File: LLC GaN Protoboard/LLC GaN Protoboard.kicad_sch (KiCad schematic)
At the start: 0 parts

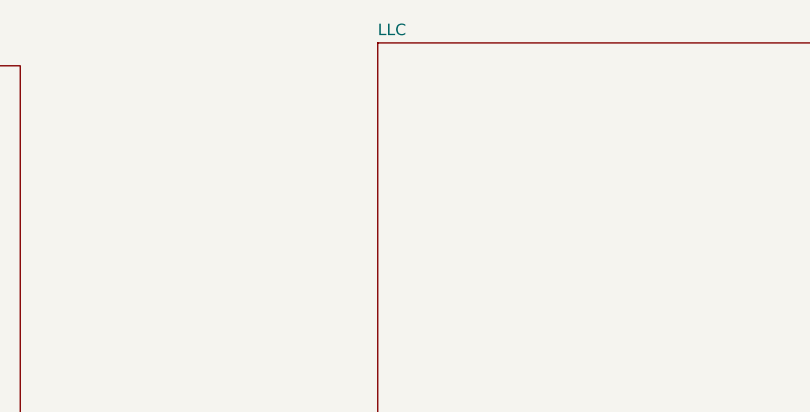
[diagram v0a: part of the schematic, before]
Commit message: Added more calculations
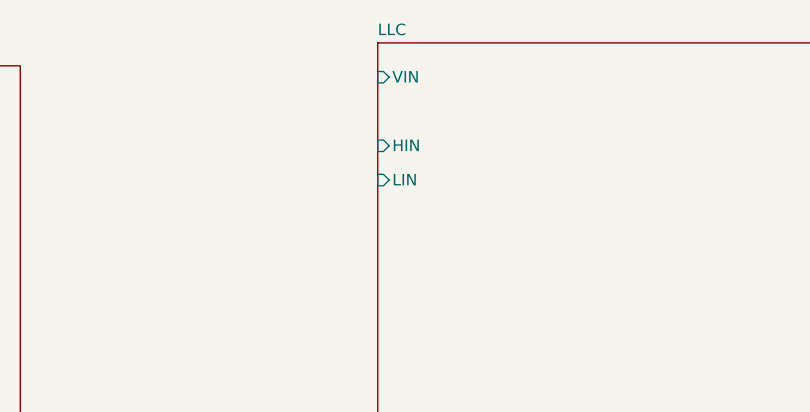
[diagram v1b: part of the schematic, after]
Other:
- sheet LLC ports: added HIN, LIN, VIN; removed none
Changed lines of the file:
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@@
+			)
+		)
+		(pin "HIN" input
+			(at 137.16 38.1 180)
+			(effects
+				(font
+					(size 1.27 1.27)
+				)
+				(justify left)
+			)
+		)
+		(pin "LIN" input
+			(at 137.16 41.91 180)
+			(effects
+				(font
+					(size 1.27 1.27)
+				)
+				(justify left)
+			)
+		)
+		(pin "VIN" input
+			(at 137.16 30.48 180)
+			(effects
+				(font
+					(size 1.27 1.27)
+				)
+				(justify left)
 			)
 		)

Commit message: Finished schematic
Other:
- sheet LLC ports: added IIN_HIGH, IIN_LOW, IOUT_HIGH, IOUT_LOW, VIN_RECT, VOUT; removed none
- sheet Mount ports: added ADCINA4/VIN, ADCINA9/IIN, ADCINB4/VOUT, ADCINB5/IOUT, PWM7A/HI, PWM7B/LO, SPIB_CLK, SPIB_PICO, SPIB_POCI; removed none
- sheet Sense ports: added ADC_IIN, ADC_IOUT, ADC_VIN, ADC_VOUT, INV_SHUNT_HIGH, INV_SHUNT_LOW, VIN, VOUT; removed none
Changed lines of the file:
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@@
 	(paper "A4")
 	(sheet
-		(at 38.1 133.35)
+		(at 34.29 144.78)
 		(size 119.38 44.45)
 		(exclude_from_sim no)
@@
 		)
 		(property "Sheetname" "Sense"
-			(at 38.1 132.6384 0)
+			(at 34.29 144.0684 0)
 			(show_name no)
 			(do_not_autoplace no)
@@
 		)
 		(property "Sheetfile" "Sense.kicad_sch"
-			(at 38.1 178.3846 0)
+			(at 34.29 189.8146 0)
 			(show_name no)
 			(do_not_autoplace no)
@@
 				)
 				(justify left top)
+			)
+		)
+		(pin "ADC_IIN" input
+			(at 34.29 147.32 180)
+			(effects
+				(font
+					(size 1.27 1.27)
+				)
+				(justify left)
+			)
+		)
+		(pin "ADC_IOUT" input
+			(at 34.29 149.86 180)
+			(effects
+				(font
+					(size 1.27 1.27)
+				)
+				(justify left)
+			)
+		)
+		(pin "ADC_VIN" input
+			(at 34.29 152.4 180)
+			(effects
+				(font
+					(size 1.27 1.27)
+				)
+				(justify left)
+			)
+		)
+		(pin "ADC_VOUT" input
+			(at 34.29 154.94 180)
+			(effects
+				(font
+					(size 1.27 1.27)
+				)
+				(justify left)
+			)
+		)
+		(pin "INV_SHUNT_HIGH" input
+			(at 34.29 157.48 180)
+			(effects
+				(font
+					(size 1.27 1.27)
+				)
+				(justify left)
+			)
+		)
+		(pin "INV_SHUNT_LOW" input
+			(at 34.29 160.02 180)
+			(effects
+				(font
+					(size 1.27 1.27)
+				)
+				(justify left)
+			)
+		)
+		(pin "VIN" input
+			(at 34.29 162.56 180)
+			(effects
+				(font
+					(size 1.27 1.27)
+				)
+				(justify left)
+			)
+		)
+		(pin "VOUT" input
+			(at 34.29 165.1 180)
+			(effects
+				(font
+					(size 1.27 1.27)
+				)
+				(justify left)
 			)
 		)
@@
 			)
 		)
+		(pin "ADCINA4{slash}VIN" input
+			(at 28.8607 40.64 180)
+			(effects
+				(font
+					(size 1.27 1.27)
+				)
+				(justify left)
+			)
+		)
+		(pin "ADCINA9{slash}IIN" input
+			(at 28.8607 43.18 180)
+			(effects
+				(font
+					(size 1.27 1.27)
+				)
+				(justify left)
+			)
+		)
+		(pin "ADCINB4{slash}VOUT" input
+			(at 28.8607 45.72 180)
+			(effects
+				(font
+					(size 1.27 1.27)
+				)
+				(justify left)
+			)
+		)
+		(pin "ADCINB5{slash}IOUT" input
+			(at 28.8607 48.26 180)
+			(effects
+				(font
+					(size 1.27 1.27)
+				)
+				(justify left)
+			)
+		)
+		(pin "PWM7A{slash}HI" input
+			(at 28.8607 50.8 180)
+			(effects
+				(font
+					(size 1.27 1.27)
+				)
+				(justify left)
+			)
+		)
+		(pin "PWM7B{slash}LO" input
+			(at 28.8607 53.34 180)
+			(effects
+				(font
+					(size 1.27 1.27)
+				)
+				(justify left)
+			)
+		)
+		(pin "SPIB_CLK" input
+			(at 28.8607 55.88 180)
+			(effects
+				(font
+					(size 1.27 1.27)
+				)
+				(justify left)
+			)
+		)
+		(pin "SPIB_PICO" input
+			(at 28.8607 58.42 180)
+			(effects
+				(font
+					(size 1.27 1.27)
+				)
+				(justify left)
+			)
+		)
+		(pin "SPIB_POCI" input
+			(at 28.8607 60.96 180)
+			(effects
+				(font
+					(size 1.27 1.27)
+				)
+				(justify left)
+			)
+		)
 		(instances
 			(project "LLC GaN Protoboard"
@@
 	)
 	(sheet
-		(at 137.16 26.67)
+		(at 172.72 26.67)
 		(size 97.79 82.55)
 		(exclude_from_sim no)
@@
 		)
 		(property "Sheetname" "LLC"
-			(at 137.16 25.9584 0)
+			(at 172.72 25.9584 0)
 			(show_name no)
 			(do_not_autoplace no)
@@
 		)
 		(property "Sheetfile" "LLC.kicad_sch"
-			(at 137.16 109.8046 0)
+			(at 172.72 109.8046 0)
 			(show_name no)
 			(do_not_autoplace no)
@@
 		)
 		(pin "HIN" input
-			(at 137.16 38.1 180)
+			(at 172.72 38.1 180)
 			(effects
 				(font
@@
 		)
 		(pin "LIN" input
-			(at 137.16 41.91 180)
+			(at 172.72 41.91 180)
 			(effects
 				(font
@@
 		)
 		(pin "VIN" input
-			(at 137.16 30.48 180)
-			(effects
-				(font
+			(at 172.72 30.48 180)
+			(effects
+				(font
+					(size 1.27 1.27)
+				)
+				(justify left)
+			)
+		)
+		(pin "IIN_HIGH" input
+			(at 172.72 44.45 180)
+			(effects
+				(font
+					(size 1.27 1.27)
+				)
+				(justify left)
+			)
+		)
+		(pin "IIN_LOW" input
+			(at 172.72 46.99 180)
+			(effects
+				(font
+					(size 1.27 1.27)
+				)
+				(justify left)
+			)
+		)
+		(pin "IOUT_HIGH" input
+			(at 172.72 49.53 180)
+			(effects
+				(font
+					(size 1.27 1.27)
+				)
+				(justify left)
+			)
+		)
+		(pin "IOUT_LOW" input
+			(at 172.72 52.07 180)
+			(effects
+				(font
+					(size 1.27 1.27)
+				)
+				(justify left)
+			)
+		)
+		(pin "VIN_RECT" input
+			(at 172.72 54.61 180)
+			(effects
+				(font
+					(size 1.27 1.27)
+				)
+				(justify left)
+			)
+		)
+		(pin "VOUT" input
+			(at 172.72 57.15 180)
+			(effects
+				(font

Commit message: Edited schematic
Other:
- sheet Mount ports: added none; removed SPIB_CLK, SPIB_PICO, SPIB_POCI
- sheet Sense ports: added IOUT_HIGH, IOUT_LOW; removed none

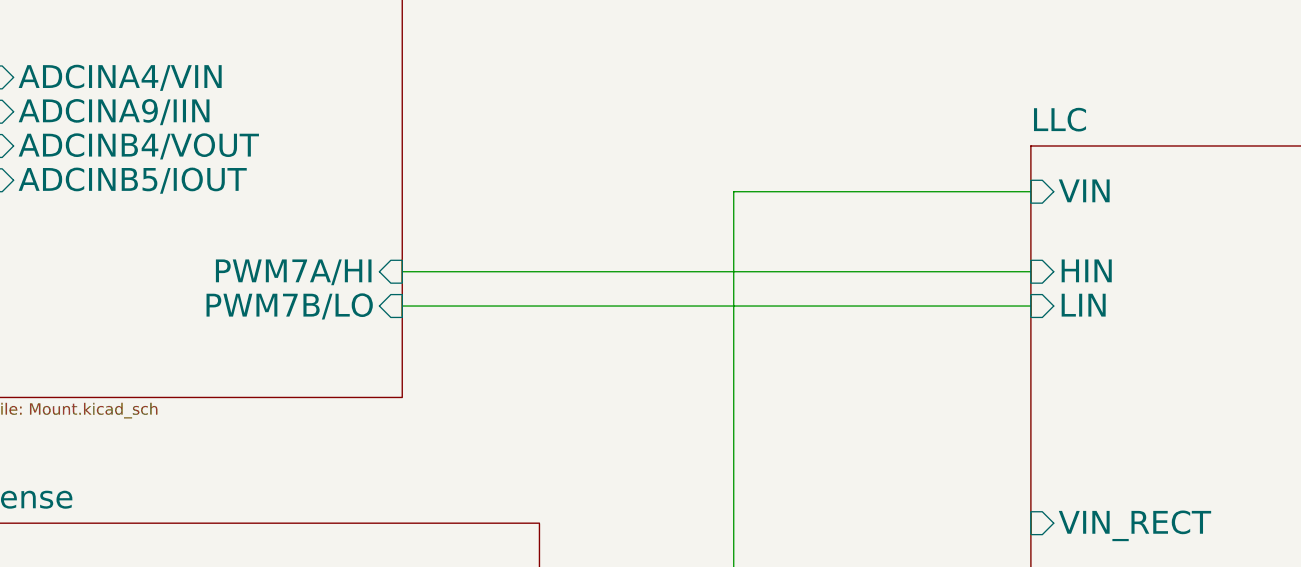
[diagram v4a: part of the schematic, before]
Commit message: Initial primary side layout
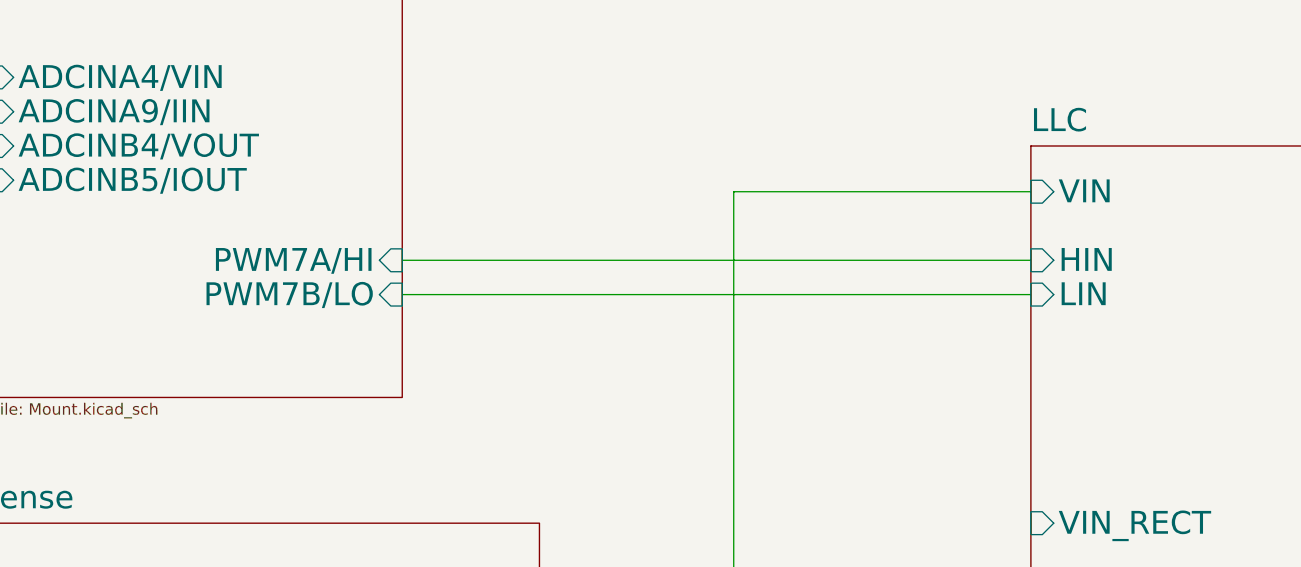
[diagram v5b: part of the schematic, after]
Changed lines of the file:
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@@
-	(wire
-		(pts
-			(xy 115.57 78.74) (xy 185.42 78.74)
-		)
-		(stroke
-			(width 0)
-			(type default)
-		)
-	)
 	(wire
 		(pts
@@
 	(wire
 		(pts
-			(xy 115.57 74.93) (xy 185.42 74.93)
+			(xy 115.5699 73.66) (xy 185.42 73.66)
 		)
 		(stroke
@@
 		(pts
 			(xy 130.81 110.49) (xy 185.42 110.49)
+		)
+		(stroke
+			(width 0)
+			(type default)
+		)
+	)
+	(wire
+		(pts
+			(xy 115.5699 77.47) (xy 185.42 77.47)
 		)
 		(stroke
@@
 		)
 		(pin "PWM7A{slash}HI" input
-			(at 115.5699 74.93 0)
+			(at 115.5699 73.66 0)
 			(effects
 				(font
@@
 		)
 		(pin "PWM7B{slash}LO" input
-			(at 115.5699 78.74 0)
+			(at 115.5699 77.47 0)
 			(effects
 				(font
@@
 		)
 		(pin "HIN" input
-			(at 185.42 74.93 180)
+			(at 185.42 73.66 180)
 			(effects
 				(font
@@
 		)
 		(pin "LIN" input
-			(at 185.42 78.74 180)
-			(effects
-				(font
+			(at 185.42 77.47 180)
+			(effects
+				(font
